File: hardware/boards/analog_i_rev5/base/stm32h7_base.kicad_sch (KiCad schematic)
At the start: 33 parts

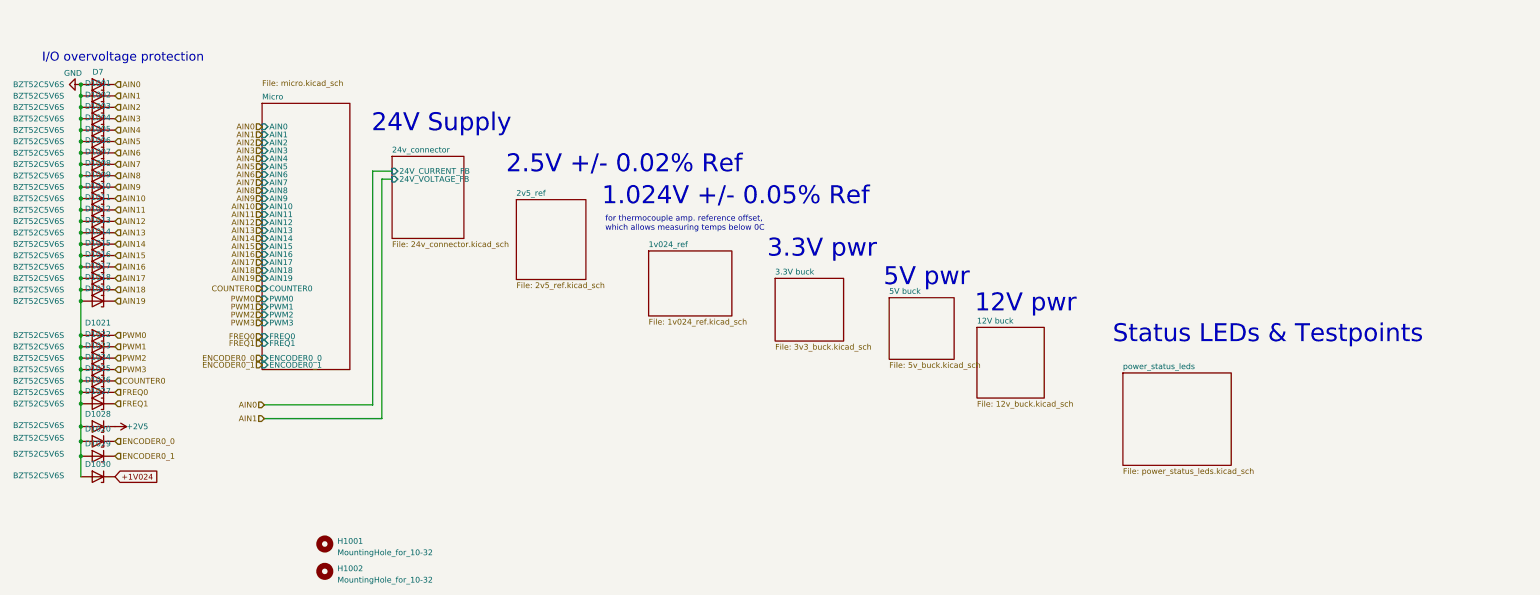
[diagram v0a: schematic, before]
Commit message: limit amp voltage outputs to 3.3V
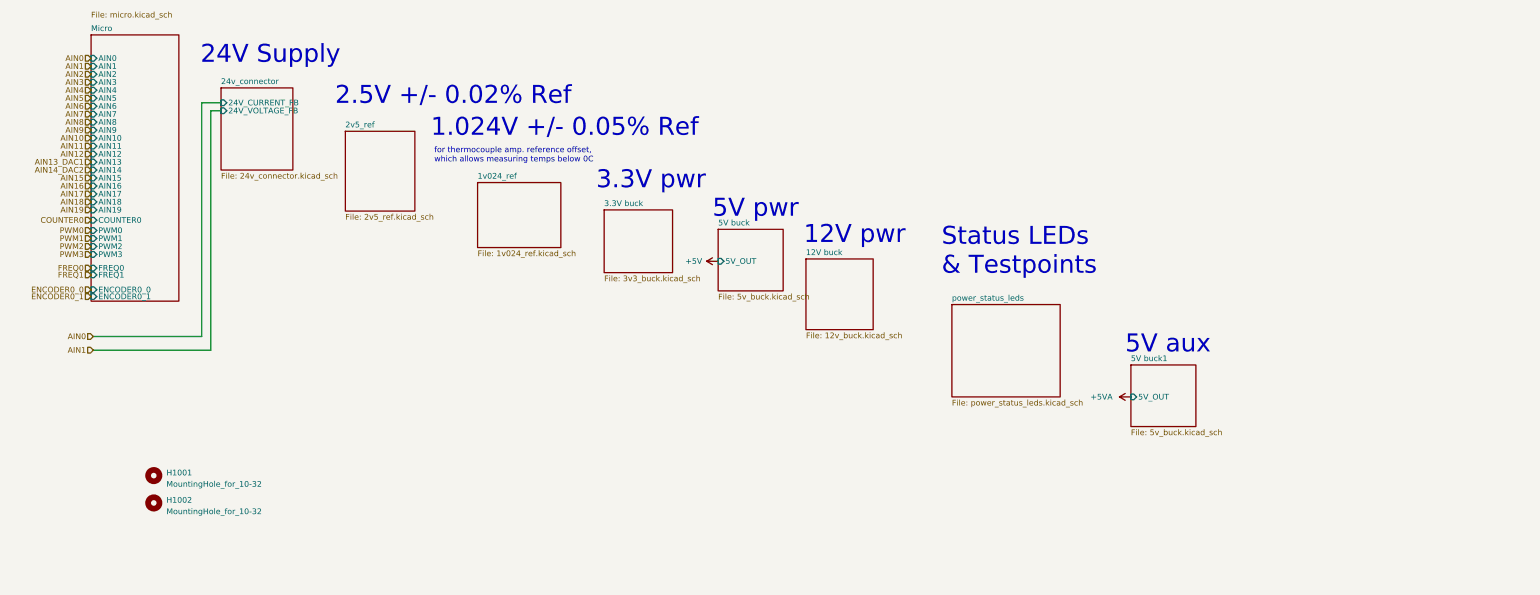
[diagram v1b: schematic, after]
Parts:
- removed D1001, D1002, D1003, D1004, D1005, D1006, D1007, D1008, D1009, D1010, D1011, D1012, D1013, D1014, D1015, D1016, D1017, D1018, D1019, D1020, D1021, D1022, D1023, D1024, D1025, D1026, D1027, D1028, D1029, D1030, D7: BZT52C5V6S, Diode_SMD:D_SOD-323, symbol Device:D_Zener
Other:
- added sheet 5V buck1 (5v_buck.kicad_sch)
- sheet 5V buck ports: added 5V_OUT; removed none
- note added: "5V aux"
- note removed: "I/O overvoltage protection"
- moved on the sheet: H1001, H1002

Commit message: eliminate 5V power rail from analog frontend so that it can be used for aux rail only
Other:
- removed sheet 5V buck1
- sheet 5V buck ports: added none; removed 5V_OUT
- note removed: "5V aux"
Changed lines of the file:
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@@
-		)
-	)
-	(text "5V aux"
-		(exclude_from_sim no)
-		(at 256.794 89.662 0)
-		(effects
-			(font
-				(size 4 4)
-			)
-			(justify left bottom)
 		)
 	)
@@
 	)
 	(symbol
-		(lib_id "power:+5VA")
-		(at 258.064 99.06 90)
-		(unit 1)
-		(exclude_from_sim no)
-		(in_bom yes)
-		(on_board yes)
-		(dnp no)
-		(fields_autoplaced yes)
-		(property "Reference" "#PWR1002"
-			(at 261.874 99.06 0)
-			(effects
-				(font
-					(size 1.27 1.27)
-				)
-				(hide yes)
-			)
-		)
-		(property "Value" "+5VA"
-			(at 254 99.0599 90)
-			(effects
-				(font
-					(size 1.27 1.27)
-				)
-				(justify left)
-			)
-		)
-		(property "Footprint" ""
-			(at 258.064 99.06 0)
-			(effects
-				(font
-					(size 1.27 1.27)
-				)
-				(hide yes)
-			)
-		)
-		(property "Datasheet" ""
-			(at 258.064 99.06 0)
-			(effects
-				(font
-					(size 1.27 1.27)
-				)
-				(hide yes)
-			)
-		)
-		(property "Description" "Power symbol creates a global label with name \"+5VA\""
-			(at 258.064 99.06 0)
-			(effects
-				(font
-					(size 1.27 1.27)
-				)
-				(hide yes)
-			)
-		)
-		(pin "1"
-		)
-		(instances
-			(project ""
-				(path "/511605a4-f92c-43a6-a2c6-3cb535ac8a8e"
-					(reference "#PWR1002")
-					(unit 1)
-				)
-			)
-		)
-	)
-	(symbol
 		(lib_id "Mechanical:MountingHole")
 		(at 40.386 122.682 0)
@@
 		)
 	)
-	(symbol
-		(lib_id "power:+5V")
-		(at 166.116 68.834 90)
-		(unit 1)
-		(exclude_from_sim no)
-		(in_bom yes)
-		(on_board yes)
-		(dnp no)
-		(fields_autoplaced yes)
-		(property "Reference" "#PWR1001"
-			(at 169.926 68.834 0)
-			(effects
-				(font
-					(size 1.27 1.27)
-				)
-				(hide yes)
-			)
-		)
-		(property "Value" "+5V"
-			(at 162.56 68.8339 90)
-			(effects
-				(font
-					(size 1.27 1.27)
-				)
-				(justify left)
-			)
-		)
-		(property "Footprint" ""
-			(at 166.116 68.834 0)
-			(effects
-				(font
-					(size 1.27 1.27)
-				)
-				(hide yes)
-			)
-		)
-		(property "Datasheet" ""
-			(at 166.116 68.834 0)
-			(effects
-				(font
-					(size 1.27 1.27)
-				)
-				(hide yes)
-			)
-		)
-		(property "Description" "Power symbol creates a global label with name \"+5V\""
-			(at 166.116 68.834 0)
-			(effects
-				(font
-					(size 1.27 1.27)
-				)
-				(hide yes)
-			)
-		)
-		(pin "1"
-		)
-		(instances
-			(project ""
-				(path "/511605a4-f92c-43a6-a2c6-3cb535ac8a8e"
-					(reference "#PWR1001")
-					(unit 1)
-				)
-			)
-		)
-	)
 	(sheet
 		(at 55.372 30.226)
@@
 	)
 	(sheet
-		(at 258.064 91.948)
-		(size 14.478 13.716)
-		(fields_autoplaced yes)
-		(stroke
-			(width 0.1524)
-			(type solid)
-		)
-		(fill
-			(color 0 0 0 0.0000)
-		)
-		(property "Sheetname" "5V buck1"
-			(at 258.064 91.2364 0)
-			(effects
-				(font
-					(size 1.27 1.27)
-				)
-				(justify left bottom)
-			)
-		)
-		(property "Sheetfile" "5v_buck.kicad_sch"
-			(at 258.064 106.2486 0)
-			(effects
-				(font
-					(size 1.27 1.27)
-				)
-				(justify left top)
-			)
-		)
-		(pin "5V_OUT" input
-			(at 258.064 99.06 180)
-			(effects
-				(font
-					(size 1.27 1.27)
-				)
-				(justify left)
-			)
-		)
-		(instances
-			(project "stm32h7_base"
-				(path "/511605a4-f92c-43a6-a2c6-3cb535ac8a8e"
-					(page "3")
-				)
-			)
-		)
-	)
-	(sheet
 		(at 83.058 39.878)
 		(size 15.494 17.78)
@@
 			)
 		)
-		(pin "5V_OUT" input
-			(at 166.116 68.834 180)
-			(effects
-				(font
-					(size 1.27 1.27)
-				)
-				(justify left)
-			)
-		)

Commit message: update base layout
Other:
- sheet Micro ports: added AIN13_DAC0, AIN14_DAC1; removed AIN13, AIN14
- note added: "Testpoints"
- note removed: "Status LEDs & Testpoints"
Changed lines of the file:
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@@
 		)
 	)
-	(text "Status LEDs \n& Testpoints"
+	(text "Testpoints"
 		(exclude_from_sim no)
 		(at 215.9 72.136 0)
@@
 		)
 	)
-	(hierarchical_label "AIN13_DAC1"
+	(hierarchical_label "AIN13_DAC0"
 		(shape input)
 		(at 26.416 46.736 180)
@@
 		)
 	)
-	(hierarchical_label "AIN14_DAC2"
+	(hierarchical_label "AIN14_DAC1"
 		(shape input)
 		(at 26.416 48.514 180)
@@
 			)
 		)
-		(pin "AIN14" input
+		(pin "AIN14_DAC1" input
 			(at 26.416 48.514 180)
 			(effects
@@
 			)
 		)
-		(pin "AIN13" input
+		(pin "AIN13_DAC0" input
 			(at 26.416 46.736 180)
 			(effects

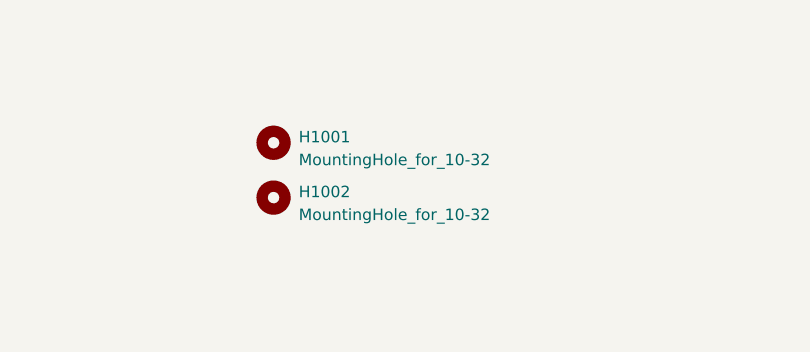
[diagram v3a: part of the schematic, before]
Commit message: build footprints for terminals
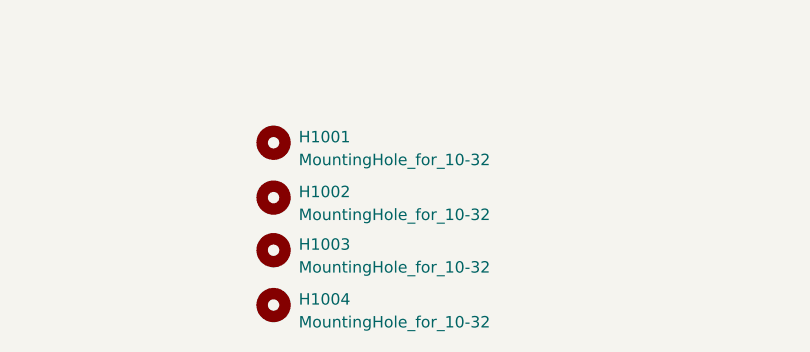
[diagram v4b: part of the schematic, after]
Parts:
- added H1003, H1004: MountingHole_for_10-32, MountingHole:MountingHole_5mm, symbol Mechanical:MountingHole
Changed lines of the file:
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@@
+		)
+	)
+	(symbol
+		(lib_id "Mechanical:MountingHole")
+		(at 40.386 134.62 0)
+		(unit 1)
+		(exclude_from_sim no)
+		(in_bom no)
+		(on_board yes)
+		(dnp no)
+		(fields_autoplaced yes)
+		(property "Reference" "H1004"
+			(at 43.18 133.985 0)
+			(effects
+				(font
+					(size 1.27 1.27)
+				)
+				(justify left)
+			)
+		)
+		(property "Value" "MountingHole_for_10-32"
+			(at 43.18 136.525 0)
+			(effects
+				(font
+					(size 1.27 1.27)
+				)
+				(justify left)
+			)
+		)
+		(property "Footprint" "MountingHole:MountingHole_5mm"
+			(at 40.386 134.62 0)
+			(effects
+				(font
+					(size 1.27 1.27)
+				)
+				(hide yes)
+			)
+		)
+		(property "Datasheet" "~"
+			(at 40.386 134.62 0)
+			(effects
+				(font
+					(size 1.27 1.27)
+				)
+				(hide yes)
+			)
+		)
+		(property "Description" ""
+			(at 40.386 134.62 0)
+			(effects
+				(font
+					(size 1.27 1.27)
+				)
+				(hide yes)
+			)
+		)
+		(instances
+			(project "stm32h7_base"
+				(path "/511605a4-f92c-43a6-a2c6-3cb535ac8a8e"
+					(reference "H1004")
+					(unit 1)
+				)
+			)
+		)
+	)
+	(symbol
+		(lib_id "Mechanical:MountingHole")
+		(at 40.386 128.524 0)
+		(unit 1)
+		(exclude_from_sim no)
+		(in_bom no)
+		(on_board yes)
+		(dnp no)
+		(fields_autoplaced yes)
+		(property "Reference" "H1003"
+			(at 43.18 127.889 0)
+			(effects
+				(font
+					(size 1.27 1.27)
+				)
+				(justify left)
+			)
+		)
+		(property "Value" "MountingHole_for_10-32"
+			(at 43.18 130.429 0)
+			(effects
+				(font
+					(size 1.27 1.27)
+				)
+				(justify left)
+			)
+		)
+		(property "Footprint" "MountingHole:MountingHole_5mm"
+			(at 40.386 128.524 0)
+			(effects
+				(font
+					(size 1.27 1.27)
+				)
+				(hide yes)
+			)
+		)
+		(property "Datasheet" "~"
+			(at 40.386 128.524 0)
+			(effects
+				(font
+					(size 1.27 1.27)
+				)
+				(hide yes)
+			)
+		)
+		(property "Description" ""
+			(at 40.386 128.524 0)
+			(effects
+				(font
+					(size 1.27 1.27)
+				)
+				(hide yes)
+			)
+		)
+		(instances
+			(project "stm32h7_base"
+				(path "/511605a4-f92c-43a6-a2c6-3cb535ac8a8e"
+					(reference "H1003")
+					(unit 1)
+				)
+			)
 		)
 	)
